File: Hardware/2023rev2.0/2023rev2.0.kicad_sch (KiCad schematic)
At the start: 104 parts

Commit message: Connecting balance and Sense to connector
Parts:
- removed BT? (x8): Battery_Cell, symbol Device:Battery_Cell
- removed D? (x7): D, symbol Device:D
- removed Q? (x7): Q_PMOS_DGS, symbol Device:Q_PMOS_DGS
- added Conn? (x2): AndersonPP, MRDT_Connectors:Square_Anderson_2_V_Side_By_Side_PV, symbol MRDT_Connectors:AndersonPP
- added D? (x8): D_Zener, Diode_SMD:D_0603_1608Metric_Pad1.05x0.95mm_HandSolder, symbol Device:D_Zener
- added D? (x7): D, symbol Device:D
- added J? (x2): Conn_01x09, MRDT_Connectors:MOLEX_SL_09_Vertical, symbol Connector_Generic:Conn_01x09
- added J?: Conn_01x04, MRDT_Connectors:MOLEX_SL_04_Vertical, symbol Connector_Generic:Conn_01x04
- added Q? (x9): Q_PMOS_DGS, symbol Device:Q_PMOS_DGS
- added Q?: Q_NMOS_DGS, symbol Device:Q_NMOS_DGS
- added R?: 3.3K, symbol Device:R
- added R?: 6.8K, symbol Device:R
- added R?: 4k, Resistor_SMD:R_0603_1608Metric_Pad0.98x0.95mm_HandSolder, symbol Device:R
- added R?: 10k, Resistor_SMD:R_0603_1608Metric_Pad0.98x0.95mm_HandSolder, symbol Device:R
- added V?: BATT_GND_VIA, MRDT_Drill_Holes:BATT_PWR_VIA, symbol MRDT_Drill_Holes:BATT_PWR_VIA
- added V? (x2): BMS_OUT_VIA, MRDT_Drill_Holes:BATT_PWR_VIA, symbol MRDT_Drill_Holes:BATT_PWR_VIA
- added V?: BATT_PWR_VIA, MRDT_Drill_Holes:BATT_PWR_VIA, symbol MRDT_Drill_Holes:BATT_PWR_VIA
- U? (x2): footprint Package_TO_SOT_SMD:SOT-23-5 -> Package_TO_SOT_SMD:SOT-23-6
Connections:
- net GND: now also D?.2 (A), R?.1, D?.2 (A), D?.2 (A), D?.2 (A), D?.2 (A), D?.2 (A), D?.2 (A), D?.2 (A), D?.2 (A), J?.1 (Pin_1), J?.1 (Pin_1), J?.4 (Pin_4), Q?.3 (S), R?.2
- net PACK_OUT: now also Q?.1 (D), Q?.1 (D), R?.1, V?.1, V?.1
- net at D?.1 (K), D?.2 (A), R?.1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: now also D?.1 (K), D?.1 (K), J?.6 (Pin_6), Q?.3 (S)
- net at D?.1 (K), D?.2 (A), R?.1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: now also D?.1 (K), D?.1 (K), J?.3 (Pin_3), Q?.3 (S)
- net at D?.1 (K), D?.2 (A), R?.1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: now also D?.1 (K), D?.1 (K), J?.2 (Pin_2), Q?.3 (S)
- net at D?.1 (K), D?.1 (K), R?.1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: now also Conn?.2 (V+Log), D?.1 (K), J?.9 (Pin_9), V?.1
- net at D?.1 (K), D?.2 (A), R?.1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: now also D?.1 (K), D?.1 (K), J?.8 (Pin_8), Q?.3 (S)
- net at D?.2 (A), T?.2 (AB): now also Q?.1 (D)
- net at D?.1 (K), D?.2 (A), R?.1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: now also D?.1 (K), D?.1 (K), J?.4 (Pin_4), Q?.3 (S)
- net at T?.2 (AB): now also D?.2 (A), Q?.1 (D) (x6)
- net at D?.1 (K), D?.2 (A), R?.1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: now also D?.1 (K), D?.1 (K), J?.5 (Pin_5), Q?.3 (S)
- net at D?.1 (K), D?.2 (A), Q?.3 (S)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: now also D?.1 (K), D?.1 (K), J?.7 (Pin_7)
- net at U?.1: now also U?.12 (MISO)
- net at Q?.1 (D), T?.2 (AB): now also D?.2 (A)
- net at U?.11 (MOSI): now also U?.1
- net C1: now reaches U?.15 (A1)
- net C1: now also Q?.2 (G)
- net C2: now reaches U?.16 (A2)
- net C2: now also Q?.2 (G)
- net C3: now reaches U?.17 (A3)
- net C3: now also Q?.2 (G)
- net C4: now reaches U?.18 (A4)
- net C4: now also Q?.2 (G)
- net C5: now reaches U?.19 (A5)
- net C5: now also Q?.2 (G)
- net C6: now reaches U?.20 (A6)
- net C6: now also Q?.2 (G)
- net C7: now reaches U?.21 (A7)
- net C7: now also Q?.2 (G)
- net C8: now reaches U?.22 (A8)
- net C8: now also Q?.2 (G)
- net at R?.1: now also Q?.3 (S)
- new net: Conn?.1 (GND), Q?.3 (S), Q?.3 (S), V?.1
- new net: J?.1 (Pin_1), Q?.2 (G)
- new net: J?.3 (Pin_3), R?.1, R?.2
- new net: Q?.2 (G), R?.2, R?.2
- new net: Q?.3 (S), R?.1
- new net: Q?.1 (D), R?.1
- new net GATE: J?.2 (Pin_2)
- new net call6: J?.4 (Pin_4)
- new net cell1: J?.9 (Pin_9)
- new net cell2: J?.8 (Pin_8)
- new net cell3: J?.7 (Pin_7)
- new net cell4: J?.6 (Pin_6)
- new net cell5: J?.5 (Pin_5)
- new net cell7: J?.3 (Pin_3)
- new net cell8: J?.2 (Pin_2)
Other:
- note added: "E-Switch"
- note added: "LED"
- moved on the sheet: D?, Q?, R?, U?, U?A, U?B, U?C

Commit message: Finished 2.0
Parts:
- removed J?: Conn_01x04, MRDT_Connectors:MOLEX_SL_04_Vertical, symbol Connector_Generic:Conn_01x04
- removed Q?: Q_PMOS_DGS, symbol Device:Q_PMOS_DGS
- removed Q?: Q_NMOS_DGS, symbol Device:Q_NMOS_DGS
- removed R?: 3.3K, symbol Device:R
- removed R?: 6.8K, symbol Device:R
- removed R?: 4k, Resistor_SMD:R_0603_1608Metric_Pad0.98x0.95mm_HandSolder, symbol Device:R
- removed R?: 10k, Resistor_SMD:R_0603_1608Metric_Pad0.98x0.95mm_HandSolder, symbol Device:R
- removed V?: BMS_OUT_VIA, MRDT_Drill_Holes:BATT_PWR_VIA, symbol MRDT_Drill_Holes:BATT_PWR_VIA
- added C? (x2): 1uF, Capacitor_THT:CP_Radial_D5.0mm_P2.50mm, symbol Device:C_Polarized_US
- added C? (x2): 22uF, Capacitor_THT:CP_Radial_D5.0mm_P2.50mm, symbol Device:C_Polarized_US
- added C? (x2): 10uF, Capacitor_THT:CP_Radial_D5.0mm_P2.50mm, symbol Device:C_Polarized_US
- added F?: Polyfuse, Fuse:Fuse_2920_7451Metric_Pad2.10x5.45mm_HandSolder, symbol Device:Polyfuse
- added J?: Conn_01x04, MRDT_Connectors:MOLEX_SL_04_Vertical, symbol Connector_Generic:Conn_01x04
- added Q?: Q_NMOS_DGS, symbol Device:Q_NMOS_DGS
- added R?: 10k, Resistor_SMD:R_0603_1608Metric_Pad0.98x0.95mm_HandSolder, symbol Device:R
- added R?: 4k, Resistor_SMD:R_0603_1608Metric_Pad0.98x0.95mm_HandSolder, symbol Device:R
- added R?: 6.8K, symbol Device:R
- added R?: 3.3K, symbol Device:R
- added SW?: SW_SPDT, MRDT_Connectors:MOLEX_SL_03_Horizontal, symbol Switch:SW_SPDT
- added U?: TSR_1-2450, Converter_DCDC:Converter_DCDC_TRACO_TSR-1_THT, symbol Regulator_Switching:TSR_1-2433
- added U?: OKI, symbol MRDT_Devices:OKI
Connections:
- net +3.3V: now also C?.1, C?.1, U?.3 (Vo)
- net +5V: now also C?.1, C?.1, U?.3 (Vout)
- net C1: now also U?.1 (TX1); no longer U?.15 (A1)
- net C2: now also U?.2 (OUT2); no longer U?.16 (A2)
- net C3: now also U?.3 (LRCLK2); no longer U?.17 (A3)
- net C4: now also U?.4 (BCLK2); no longer U?.18 (A4)
- net C5: now also U?.5 (IN2); no longer U?.19 (A5)
- net C6: now also U?.6 (OUT1D); no longer U?.20 (A6)
- net C7: now also U?.7 (RX2); no longer U?.21 (A7)
- net C8: now also U?.8 (TX2); no longer U?.22 (A8)
- net GATE: now also U?.41 (A17), J?.2 (Pin_2)
- net GND: now also C?.2, C?.2, C?.2, C?.2, C?.2, C?.2, J?.4 (Pin_4), Q?.3 (S), R?.1, U?.2 (GND), U?.2 (GND)
- net PACK_OUT: now also R?.1, R?.2, R?.2
- net at J?.2 (Pin_2): now also U?.21 (A7)
- net at Q?.2 (G): now also R?.2, R?.2
- net at Q?.3 (S), R?.1: now also F?.1
- net at Q?.2 (G): now also U?.0 (RX1)
- net at R?.1, R?.1: now also U?.19 (A5)
- net at Q?.2 (G), R?.2: now also U?.20 (A6)
- net ERR_LED: no longer names the net of R?.2
- net ERR_LED: now also U?.22 (A8)
- new net: Q?.1 (D), R?.1
- new net: J?.1 (Pin_1), Q?.2 (G)
- new net: C?.1, C?.1, SW?.2 (B), U?.1 (Vi), U?.1 (Vin)
- new net: J?.3 (Pin_3), R?.1
- new net: F?.2, SW?.1 (A)
- no-connect marks 0 -> 1
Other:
- note added: "0-8 PWM pins"
- note added: "Auxiliary Power"
- note added: "Bidirectional Current Sense"
- note added: "Cell Sense"
- note added: "E-Stop"
- note added: "Transformer Balance Circuit"
- note removed: "E-Switch"
- moved on the sheet: BZ?, Conn?A, Conn?B, D?, J?, Q?, R?, T?, U?, U?A, U?B, U?C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

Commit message: Begun 2.0 layout
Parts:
- U1: renamed from U?; footprint MODULE_DEV-16771 -> MRDT_Shields:Teensy_4_1
- U2, U3, U4, U5: renamed from U?; footprint (none) -> Package_SO:SO-8_3.9x4.9mm_P1.27mm
- gave numbers to parts that had none: 118

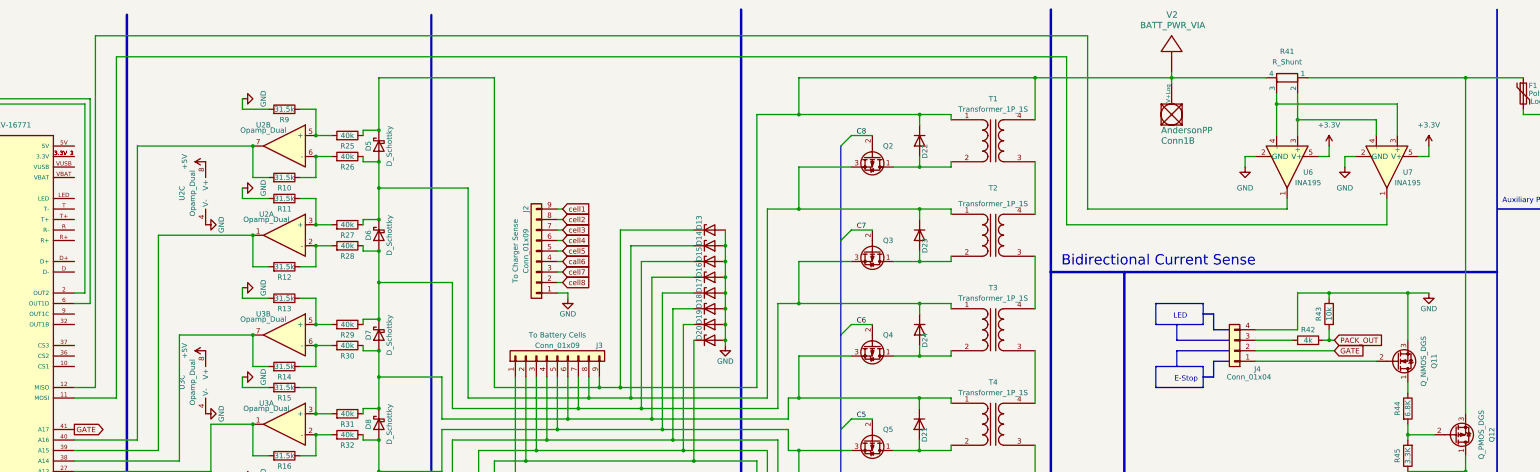
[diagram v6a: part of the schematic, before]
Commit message: change current sense config
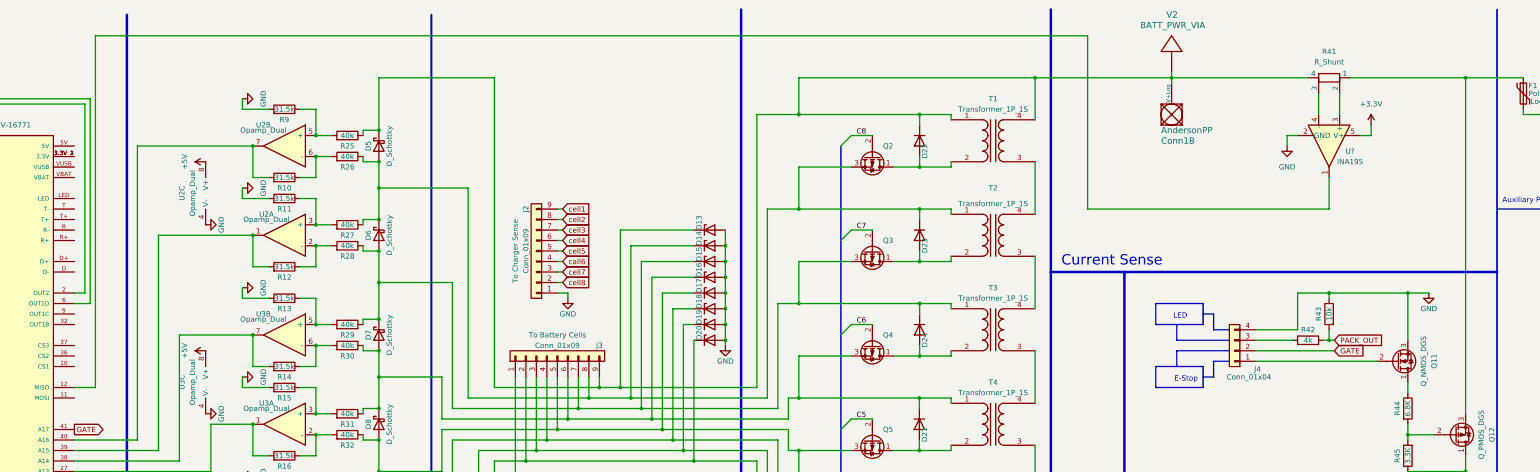
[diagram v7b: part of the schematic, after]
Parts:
- removed U6, U7: INA195, Package_TO_SOT_SMD:SOT-23-6, symbol Amplifier_Current:INA195
- added U?: INA195, Package_TO_SOT_SMD:SOT-23-6, symbol Amplifier_Current:INA195
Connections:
- net +3.3V: now also U?.5 (V+)
- net GND: now also U?.2 (GND)
- net at U1.12 (MISO): now also U?.1
- net at R41.2: now also U?.3 (+)
- net at R41.3: now also U?.4 (-)
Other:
- note added: "Current Sense"
- note removed: "Bidirectional Current Sense"
- moved on the sheet: R41

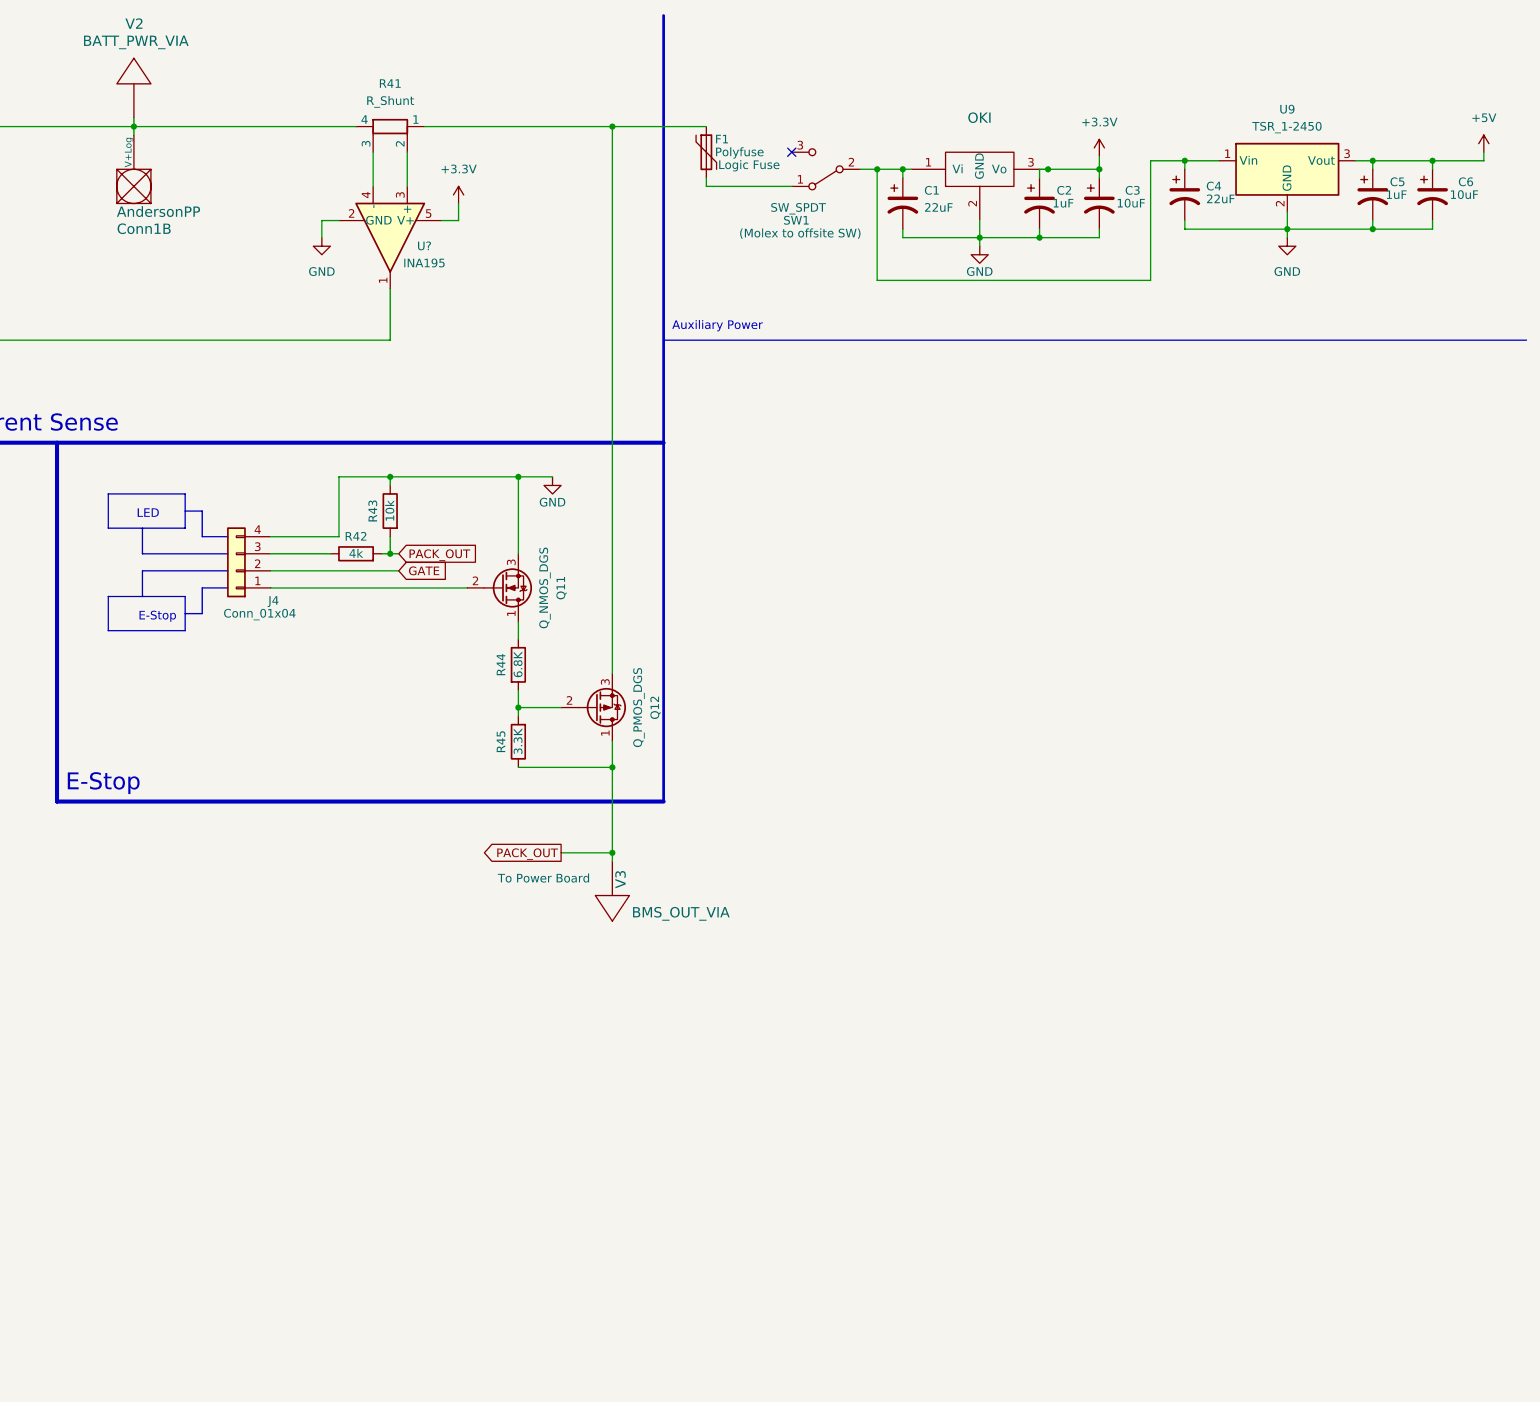
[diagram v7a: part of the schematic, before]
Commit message: Start Placing Mounting Holes
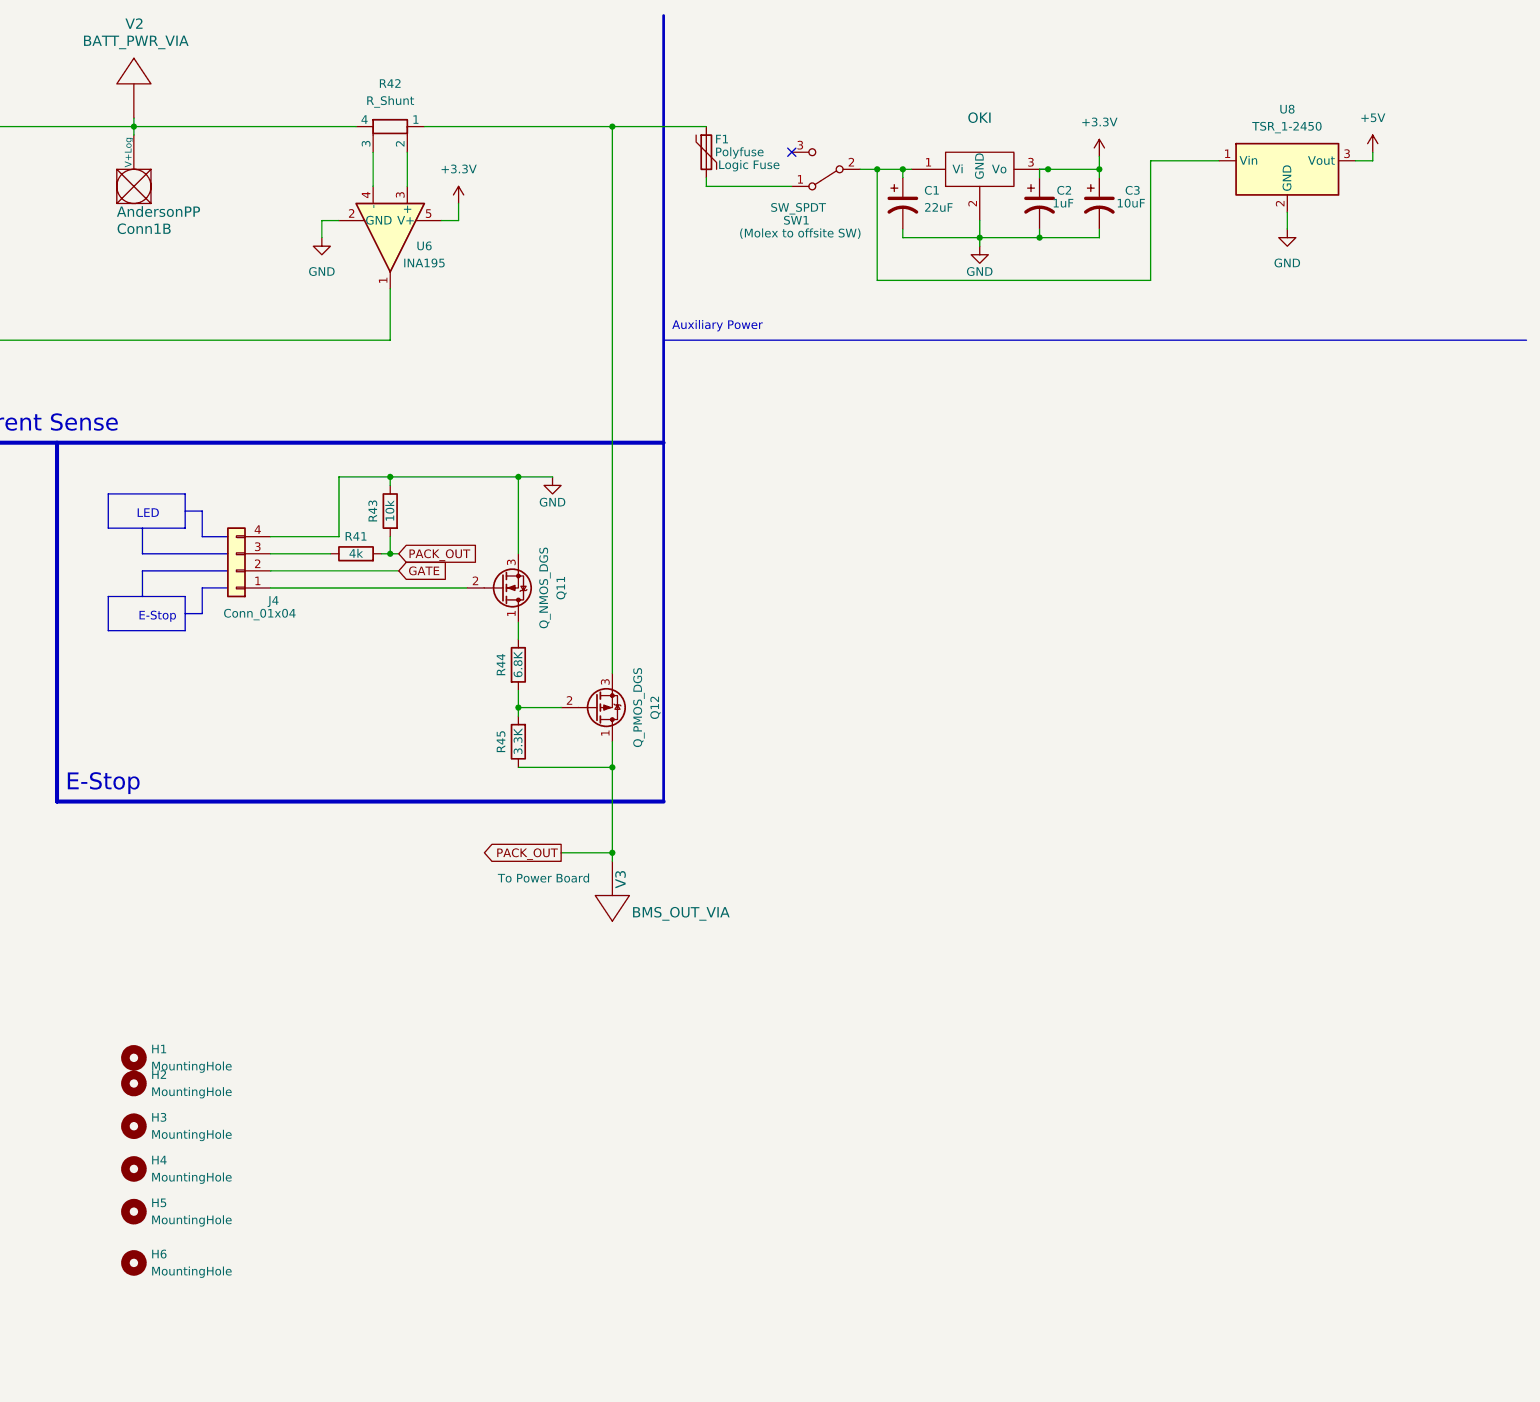
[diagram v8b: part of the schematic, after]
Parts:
- removed C4: 22uF, Capacitor_THT:CP_Radial_D5.0mm_P2.50mm, symbol Device:C_Polarized_US
- removed C5: 1uF, Capacitor_THT:CP_Radial_D5.0mm_P2.50mm, symbol Device:C_Polarized_US
- removed C6: 10uF, Capacitor_THT:CP_Radial_D5.0mm_P2.50mm, symbol Device:C_Polarized_US
- added H1, H2, H3, H4, H5, H6: MountingHole, MRDT_Drill_Holes:4_40_Hole, symbol Mechanical:MountingHole
- gave numbers to parts that had none: 1
- renumbered R42 to R41, R41 to R42, U8 to U7, U9 to U8
